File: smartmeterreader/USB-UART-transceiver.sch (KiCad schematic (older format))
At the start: 6 parts

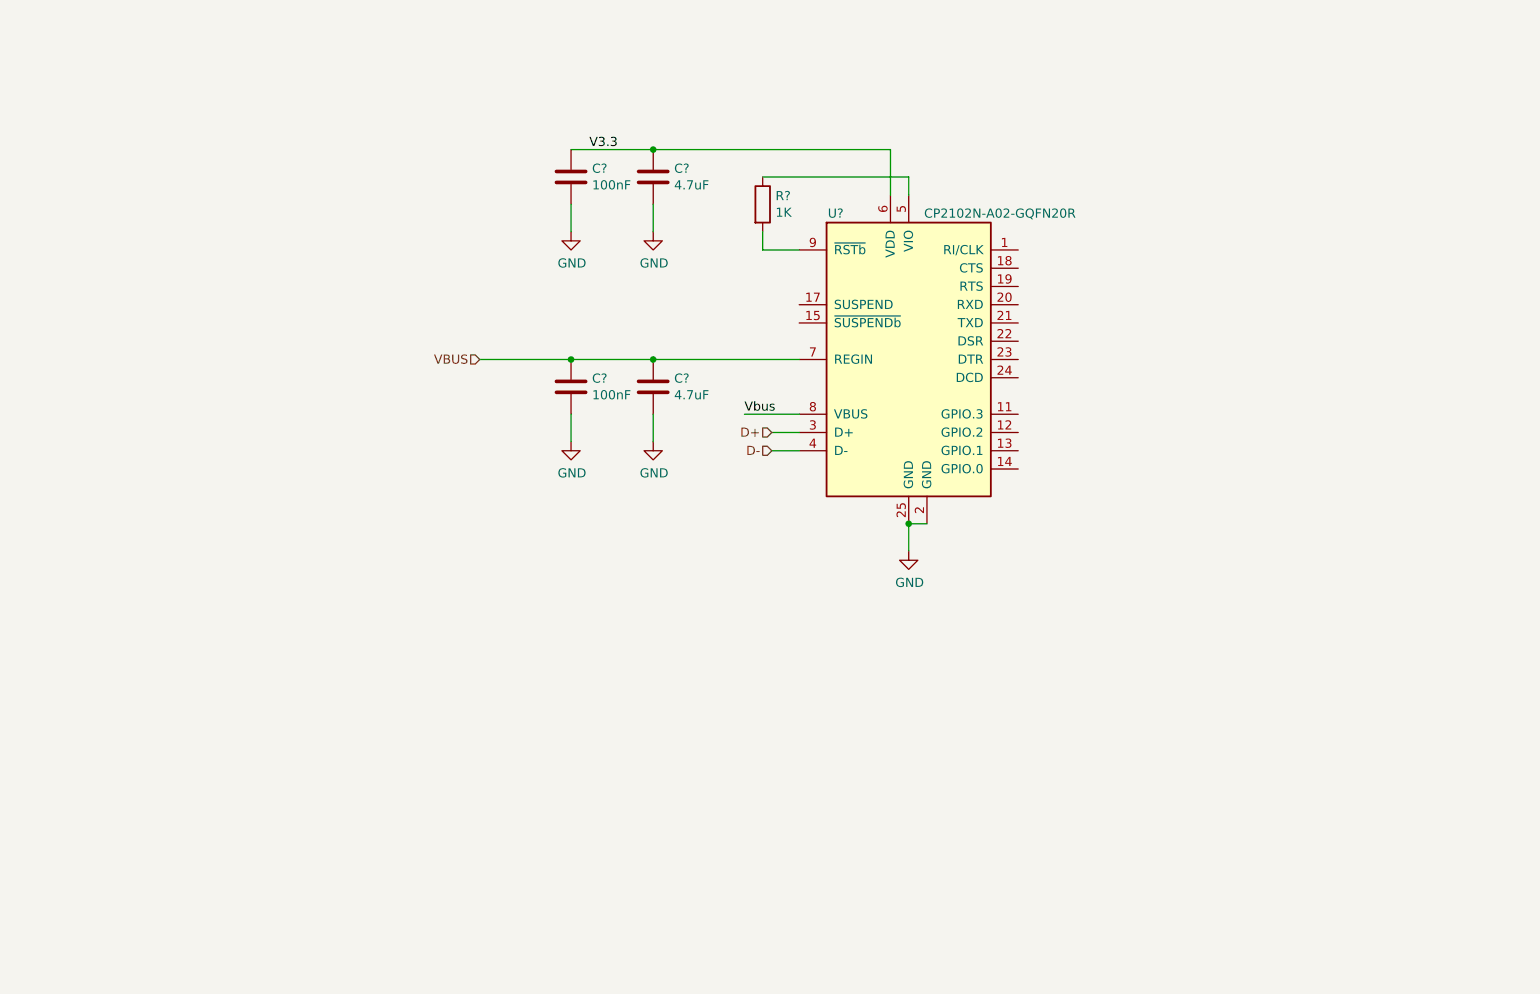
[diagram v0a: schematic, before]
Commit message: Initial version of the smart meter. -Needs compoonent review, - Needs schematics review - No layout
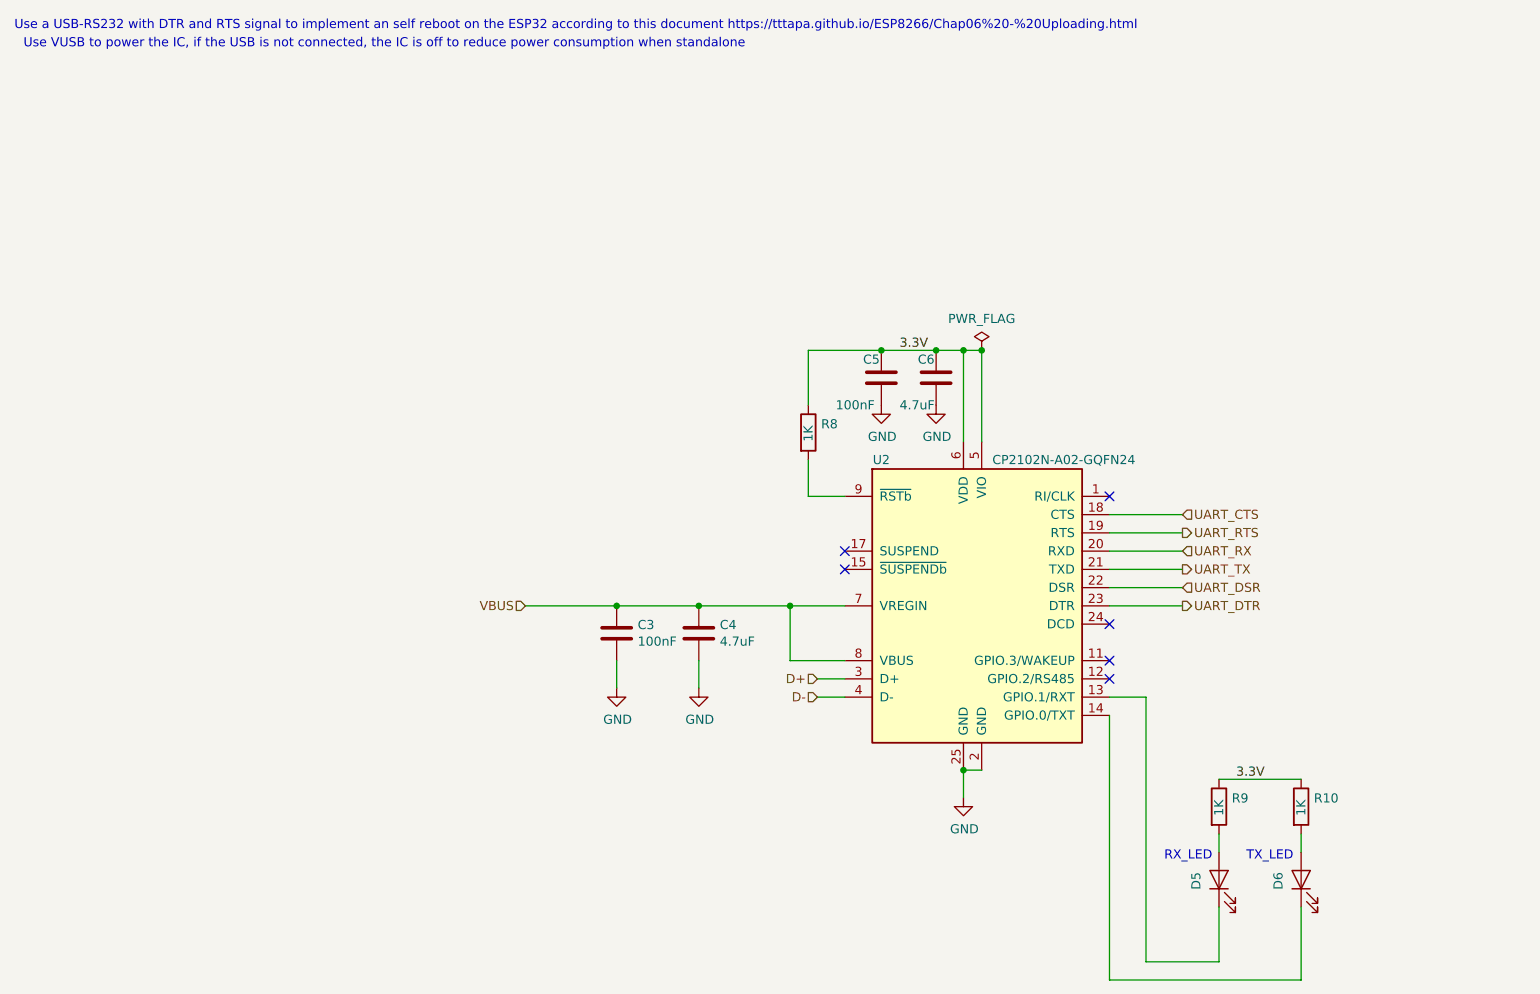
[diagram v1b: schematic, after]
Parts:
- removed C?: 100nF, Capacitor_SMD:C_0603_1608Metric_Pad1.05x0.95mm_HandSolder, symbol Capacitor_Ceramic_SMD_0603:100nF
- removed C?: 4.7uF, Capacitor_SMD:C_0805_2012Metric, symbol Capacitor_Ceramic_SMD_0603:4.7uF
- removed U?: CP2102N-A02-GQFN20R, Package_DFN_QFN:QFN-24-1EP_4x4mm_P0.5mm_EP2.6x2.6mm, symbol Interface_USB:CP2102N-A01-GQFN24
- added C5: 100nF, Capacitor_SMD:C_0603_1608Metric_Pad1.08x0.95mm_HandSolder, symbol Capacitor_Ceramic_SMD_0603:100nF
- added C6: 4.7uF, Capacitor_SMD:C_0805_2012Metric, symbol Capacitor_Ceramic_SMD_0603:4.7uF
- added D5, D6: Green, LED_SMD:LED_0603_1608Metric, symbol OPTO_LED_0603:Green
- added R10, R9: 1K, Resistor_SMD:R_0603_1608Metric, symbol Resistor_SMD_0603:1K
- added U2: CP2102N-A02-GQFN24, Package_DFN_QFN:QFN-24-1EP_4x4mm_P0.5mm_EP2.6x2.6mm, symbol IC_Digital:CP2102N-A02-GQFN24
- C3: renamed from C?; footprint Capacitor_SMD:C_0603_1608Metric_Pad1.05x0.95mm_HandSolder -> Capacitor_SMD:C_0603_1608Metric_Pad1.08x0.95mm_HandSolder
- gave numbers to parts that had none: 2
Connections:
- net D+: now also U2.3 (D+)
- net D-: now also U2.4 (D-)
- net GND: now also C5.2, C6.2, U2.2 (GND), U2.25 (GND)
- net VBUS: now also U2.7 (VREGIN), U2.8 (VBUS)
- net 3.3V: now reaches R8.1
- net 3.3V: now also C5.1, C6.1, R10.1, R9.1, U2.5 (VIO), U2.6 (VDD)
- net at R8.2: now also U2.9 (~RSTb)
- new net: D5.1 (K), U2.13 (GPIO.1/RXT)
- new net: D6.1 (K), U2.14 (GPIO.0/TXT)
- new net: D6.2 (A), R10.2
- new net: D5.2 (A), R9.2
- new net UART_CTS: U2.18 (CTS)
- new net UART_DSR: U2.22 (DSR)
- new net UART_DTR: U2.23 (DTR)
- new net UART_RTS: U2.19 (RTS)
- new net UART_RX: U2.20 (RXD)
- new net UART_TX: U2.21 (TXD)
- no-connect marks 0 -> 6
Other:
- note added: "RX_LED"
- note added: "TX_LED"
- note added: "Use VUSB to power the IC, if the USB is not connected, the IC is off to reduce power consumption when standalone\n"
- note added: "Use a USB-RS232 with DTR and RTS signal to implement an self reboot on the ESP32 according to this document https://tttapa.github.io/ESP8266/Chap06%20-%20Uploading.html"
- moved on the sheet: C3, C4, R8
